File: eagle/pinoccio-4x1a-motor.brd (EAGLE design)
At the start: 25.4 x 43.2 mm, 27 parts, among them IC1 74LVC1G04DBV, IC2 74LVC1G04DBV, IC3 74LVC1G04DBV, IC4 74LVC1G04DBV, J1 POWER_JACKPTH, U1 TB6621FNG, U2 TB6621FNG

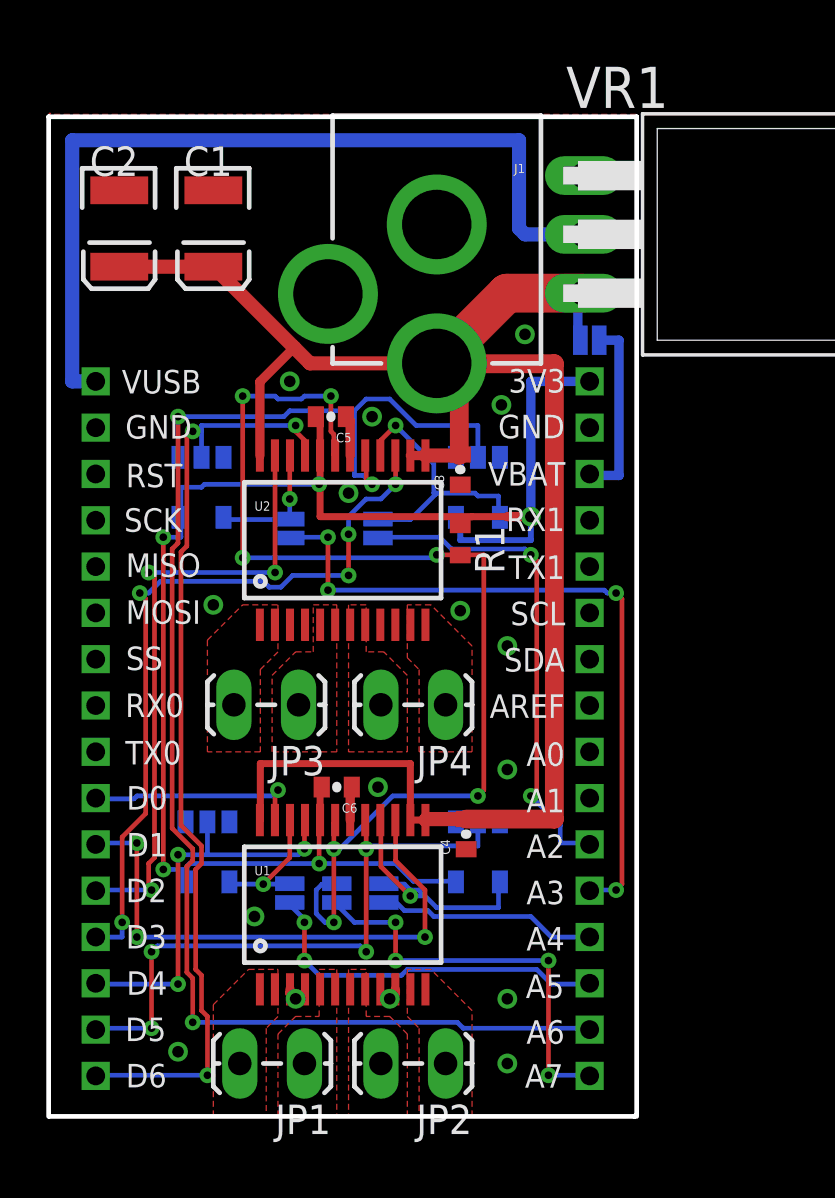
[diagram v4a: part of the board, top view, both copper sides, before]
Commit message: Add Atiny13 backpack ID chip. Connect LED and backpack standby to unused GPIO pins on the ATiny13.
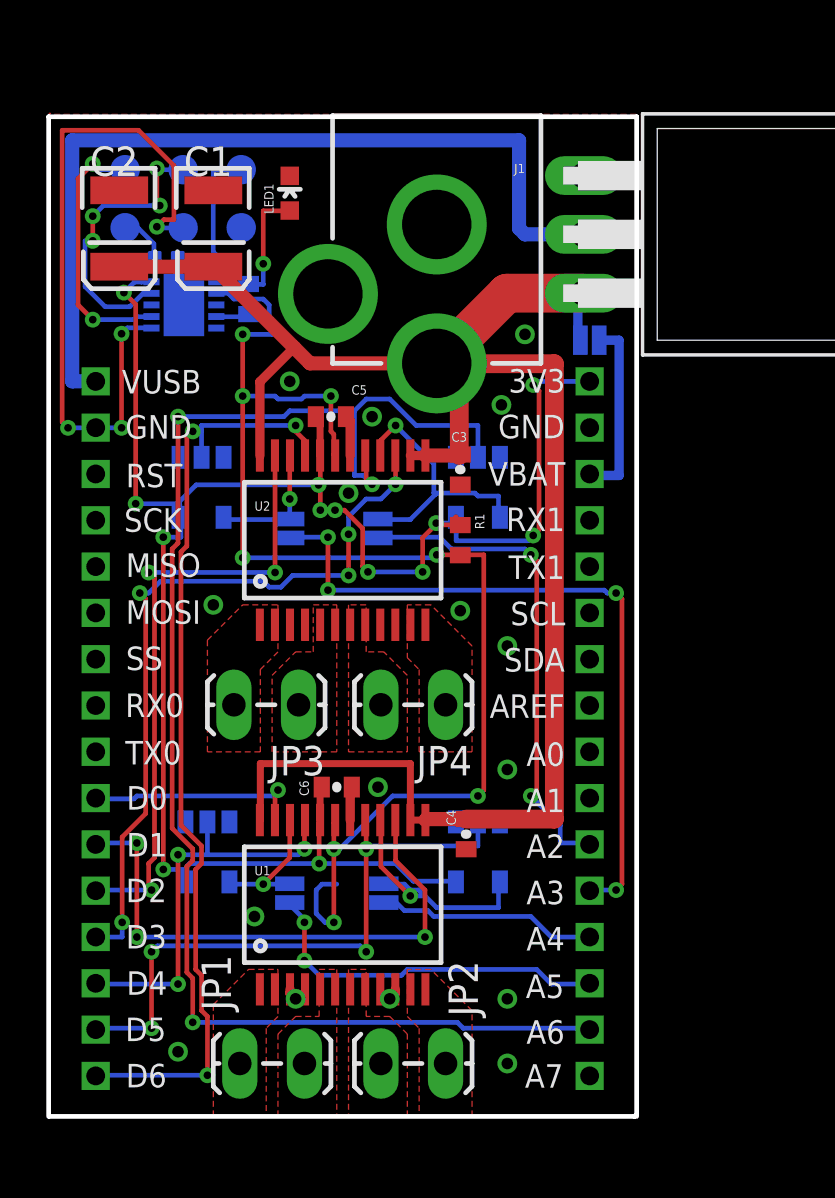
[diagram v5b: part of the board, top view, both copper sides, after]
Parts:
- removed SJ5: SOLDERJUMPERNC2, SparkFun-Passives:SJ_2S-NOTRACE
- added C7: 0.1uf, Pinoccio:0402-CAP
- added J2: AVR_SPI_PRG_6, Pinoccio:2X3-PAD
- added LED1: (no value), SparkFun-LED:LED-0603
- added R2: 10k, rcl:R0402
- added U$3: ATTINY13QFN10, Pinoccio:QFN-10
- U1, U2: value TB6621FNG -> TB6612FNG
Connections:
- new net N$1: R2.1, U$3.4
- new net N$2: J2.1, U$3.7
- new net N$3: J2.3, U$3.9
- new net N$4: J2.5, U$3.1
- new net N$5: LED1.A, R2.2
- net A7: no longer SJ5.2
- net BKPK-BUS: now also J2.4, U$3.6
- net GND: now also C7.2, J2.6, LED1.C, U$3.5, U$3.EP
- net STBY: now also U$3.2; no longer SJ5.1
- net VCC-AE: now also C7.1, J2.2, U$3.10
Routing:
- net BKPK-BUS: track 0.00 -> 30.6 mm, vias 0 -> 4
- net A7: track 18.0 -> 0.00 mm, vias 4 -> 0
- net VCC-AE: track 68.9 -> 85.8 mm, vias 5 -> 13
- net N$3: track 0.00 -> 12.7 mm, vias 0 -> 4
- net N$2: track 0.00 -> 11.3 mm, vias 0 -> 2
- net STBY: track 49.1 -> 56.8 mm, vias 7 -> 8
- net N$4: track 0.00 -> 6.10 mm
- net N$5: track 0.00 -> 4.98 mm, vias 0 -> 1
- net GND: track 4.22 -> 6.55 mm
- net N$1: track 0.00 -> 1.46 mm

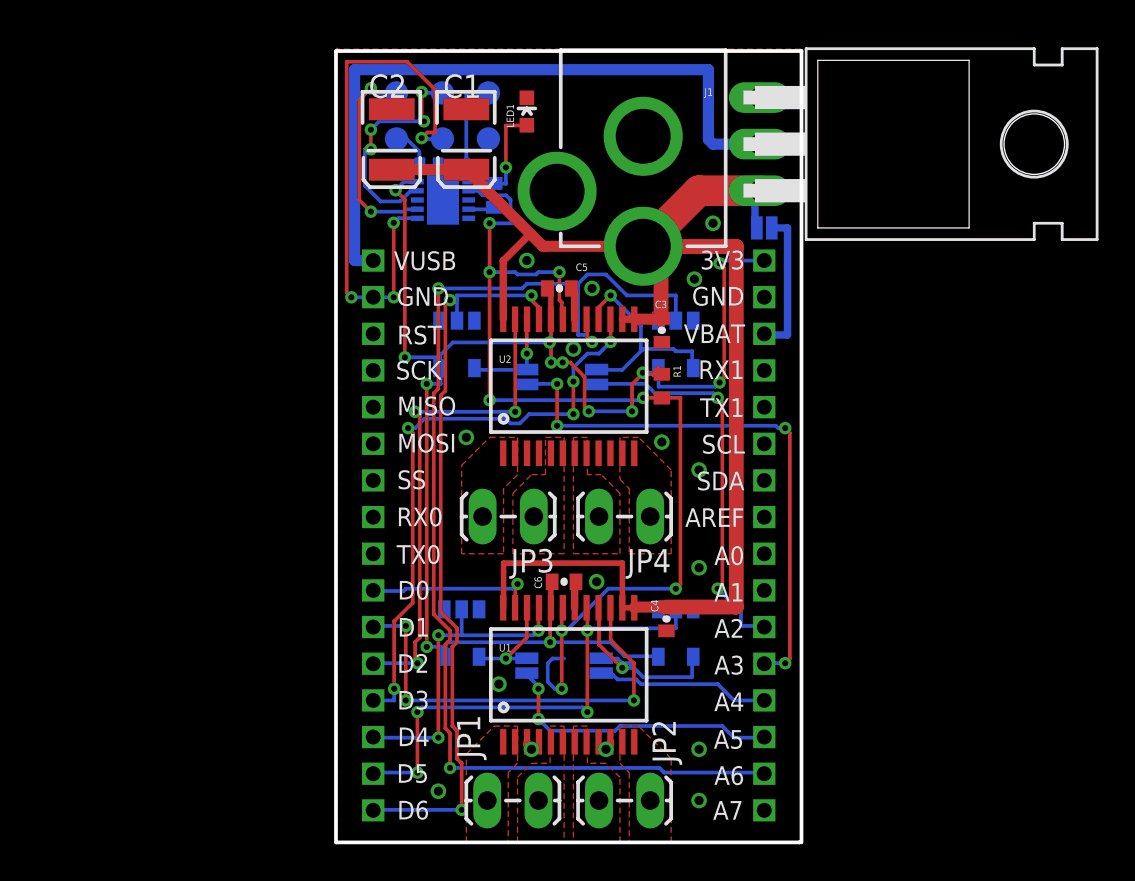
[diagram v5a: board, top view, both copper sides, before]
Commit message: Move components around to accommodate required standard position of the backpack programming pads.
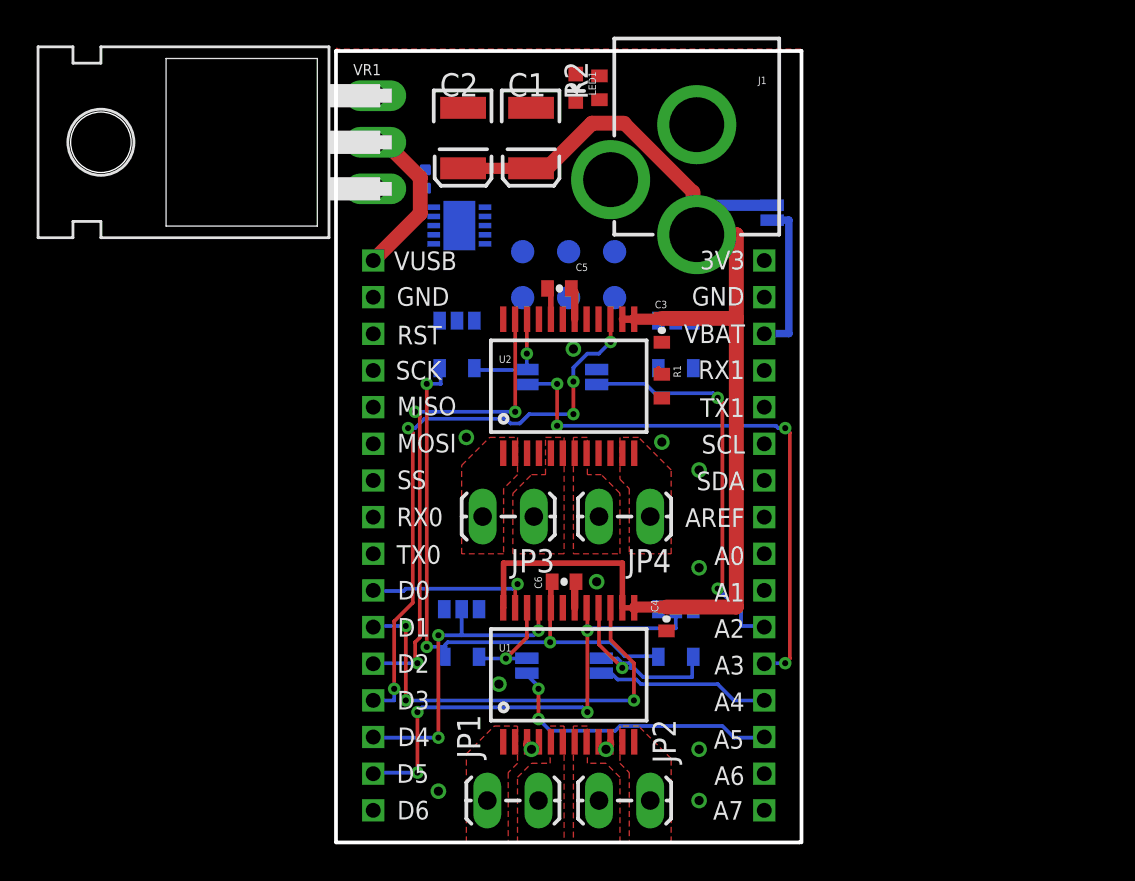
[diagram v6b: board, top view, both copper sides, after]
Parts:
- moved VR1 41.3 mm to (-8.00, 45.8), turned to 90 degrees
- moved J2 11.1 mm to (10.2, 39.9)
- moved R2 8.21 mm to (14.4, 48.8), flipped to the top
- moved C2 3.89 mm to (6.93, 46.1)
- moved C1 3.53 mm to (10.6, 46.1)
- moved J1 2.99 mm to (19.7, 54.5)
- moved LED1 2.96 mm to (13.1, 48.8), turned to 180 degrees
- moved U$3 1.66 mm to (6.73, 41.3)
- moved SJ6 0.94 mm to (23.8, 42.0), turned to 270 degrees
- moved C7 0.91 mm to (4.88, 43.8), turned to 90 degrees
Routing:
- net A6: track 64.3 -> 0.00 mm, vias 3 -> 0
- net STBY: track 56.8 -> 0.00 mm, vias 8 -> 0
- net VCC-AE: track 85.8 -> 35.3 mm, vias 13 -> 3
- net D6: track 40.8 -> 0.00 mm, vias 3 -> 0
- net BKPK-BUS: track 30.6 -> 0.00 mm, vias 4 -> 0
- net VUSB: track 37.4 -> 8.82 mm
- net N$3: track 12.7 -> 0.00 mm, vias 4 -> 0
- net 2B2: track 12.0 -> 0.00 mm, vias 1 -> 0
- net N$2: track 11.3 -> 0.00 mm, vias 2 -> 0
- net V+: track 80.9 -> 69.6 mm
- net N$4: track 6.10 -> 0.00 mm
- net N$5: track 4.98 -> 0.00 mm, vias 1 -> 0
- net GND: track 6.55 -> 4.26 mm, vias 16 -> 12
- net N$1: track 1.46 -> 0.00 mm

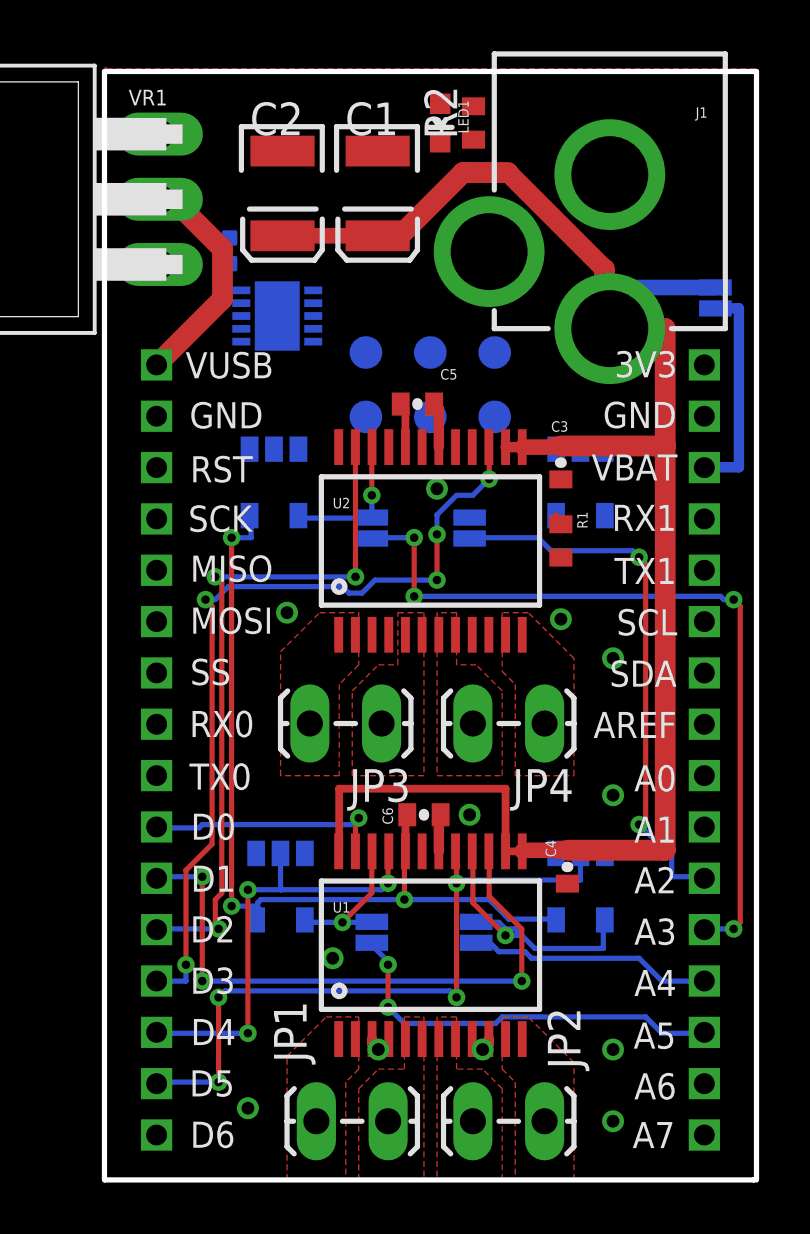
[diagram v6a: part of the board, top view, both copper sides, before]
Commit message: Tru ripping up all the autorouted signals before rerouting.
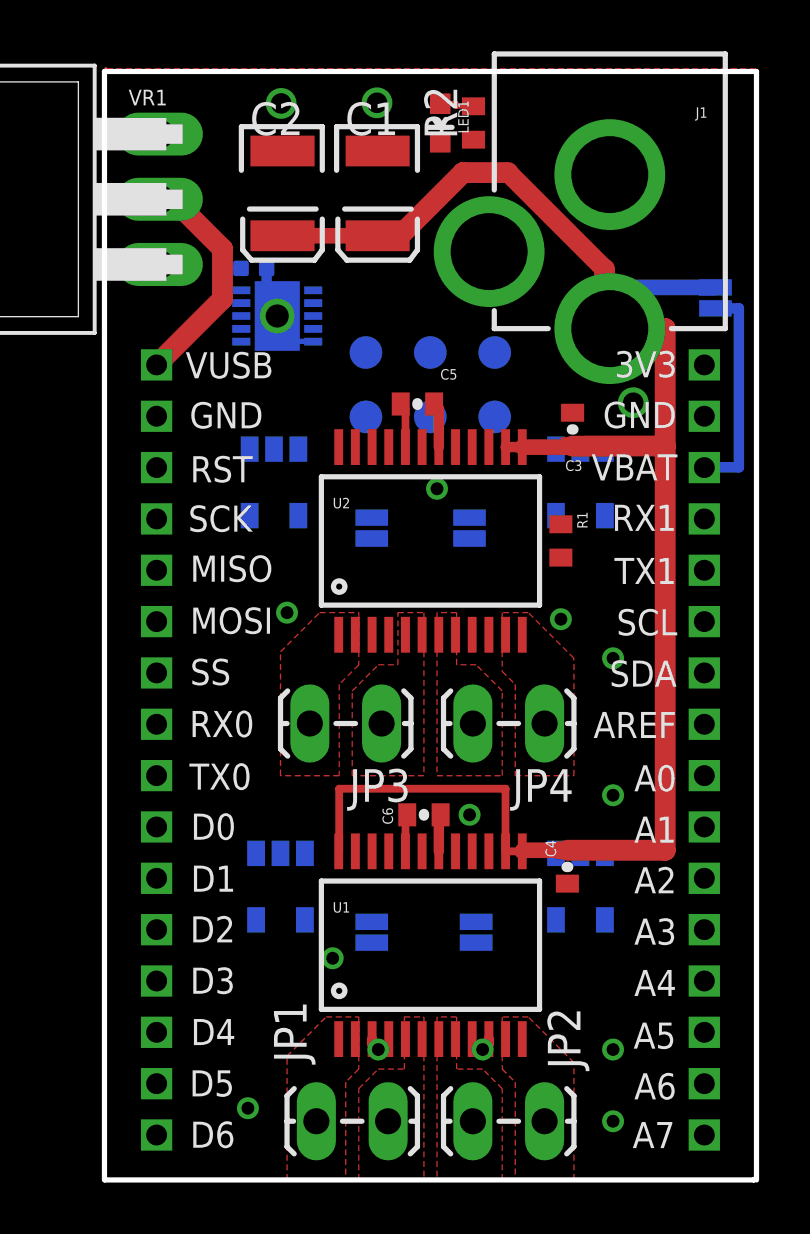
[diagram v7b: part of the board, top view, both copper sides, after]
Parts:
- moved C3 1.37 mm to (18.2, 36.9), turned to 270 degrees
- moved C7 1.16 mm to (5.82, 43.1), turned to 180 degrees
- renumbered U$3 to UID
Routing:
- net D3: track 32.5 -> 0.00 mm, vias 5 -> 0
- net A3: track 30.7 -> 0.00 mm, vias 4 -> 0
- net VCC-AE: track 35.3 -> 5.16 mm, vias 3 -> 0
- net D2: track 26.9 -> 0.00 mm, vias 3 -> 0
- net D5: track 26.9 -> 0.00 mm, vias 4 -> 0
- net D1: track 23.9 -> 0.00 mm, vias 3 -> 0
- net A2: track 21.5 -> 0.00 mm, vias 2 -> 0
- net D4: track 17.4 -> 0.00 mm, vias 3 -> 0
- net A5: track 15.8 -> 0.00 mm, vias 2 -> 0
- net 1B2: track 10.9 -> 0.00 mm, vias 1 -> 0
- net A4: track 9.56 -> 0.00 mm
- net D0: track 9.42 -> 0.00 mm, vias 1 -> 0
- net 1A2: track 5.92 -> 0.00 mm, vias 1 -> 0
- net 2A2: track 5.68 -> 0.00 mm, vias 1 -> 0
- net GND: track 4.26 -> 8.50 mm, vias 12 -> 16
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
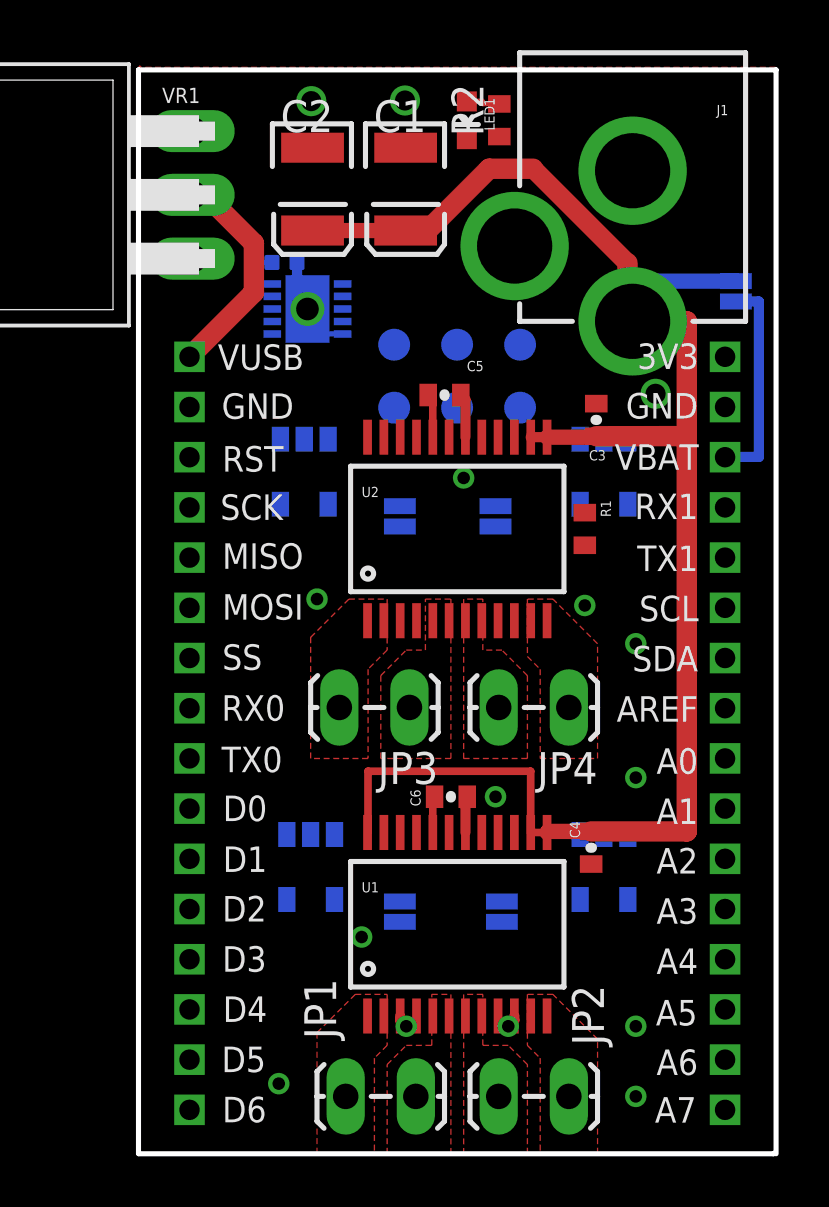
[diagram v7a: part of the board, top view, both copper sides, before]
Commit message: Successful reroute with rearranged components. Note there is now a via under the ground pad for the ATtiny13. This should actually make it easier to hand solder.
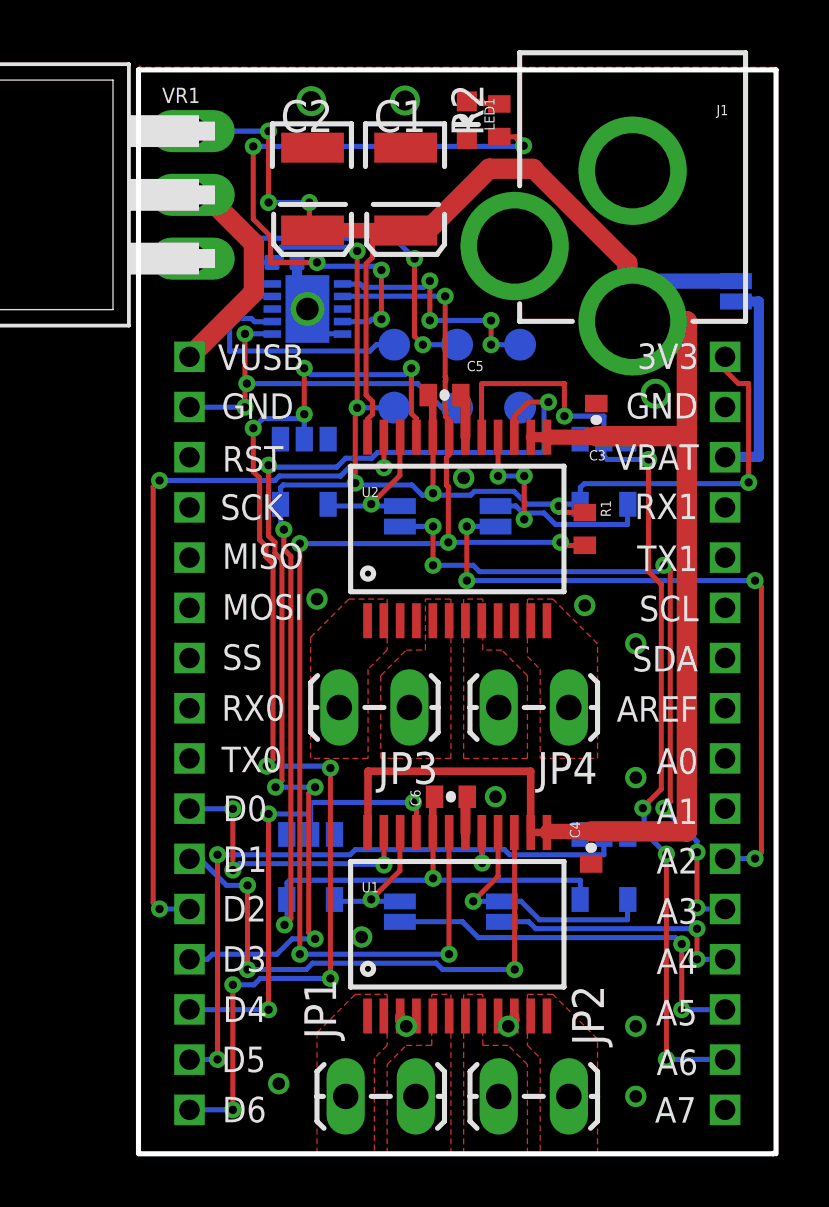
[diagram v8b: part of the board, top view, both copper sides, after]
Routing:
- net VCC-AE: track 5.16 -> 83.2 mm, vias 0 -> 9
- net STBY: track 0.00 -> 52.7 mm, vias 0 -> 6
- net D6: track 0.00 -> 48.0 mm, vias 0 -> 9
- net D3: track 0.00 -> 42.1 mm, vias 0 -> 5
- net A6: track 0.00 -> 38.9 mm, vias 0 -> 5
- net D2: track 0.00 -> 28.9 mm, vias 0 -> 3
- net A3: track 0.00 -> 27.8 mm, vias 0 -> 6
- net D5: track 0.00 -> 27.4 mm, vias 0 -> 3
- net A2: track 0.00 -> 27.3 mm, vias 0 -> 4
- net N$1: track 0.00 -> 24.9 mm, vias 0 -> 5
- net D1: track 0.00 -> 22.5 mm, vias 0 -> 3
- net D4: track 0.00 -> 19.2 mm, vias 0 -> 3
- net V+: track 69.6 -> 86.7 mm, vias 0 -> 3
- net A5: track 0.00 -> 16.0 mm, vias 0 -> 2
- net BKPK-BUS: track 0.00 -> 15.1 mm, vias 0 -> 3
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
